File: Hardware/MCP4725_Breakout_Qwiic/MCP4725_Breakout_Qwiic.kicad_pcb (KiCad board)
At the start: 2 copper layers, 15.6 x 15.6 mm, 37 parts, among them J1 Conn_01x02, J2 I2C, U2 MCP4725

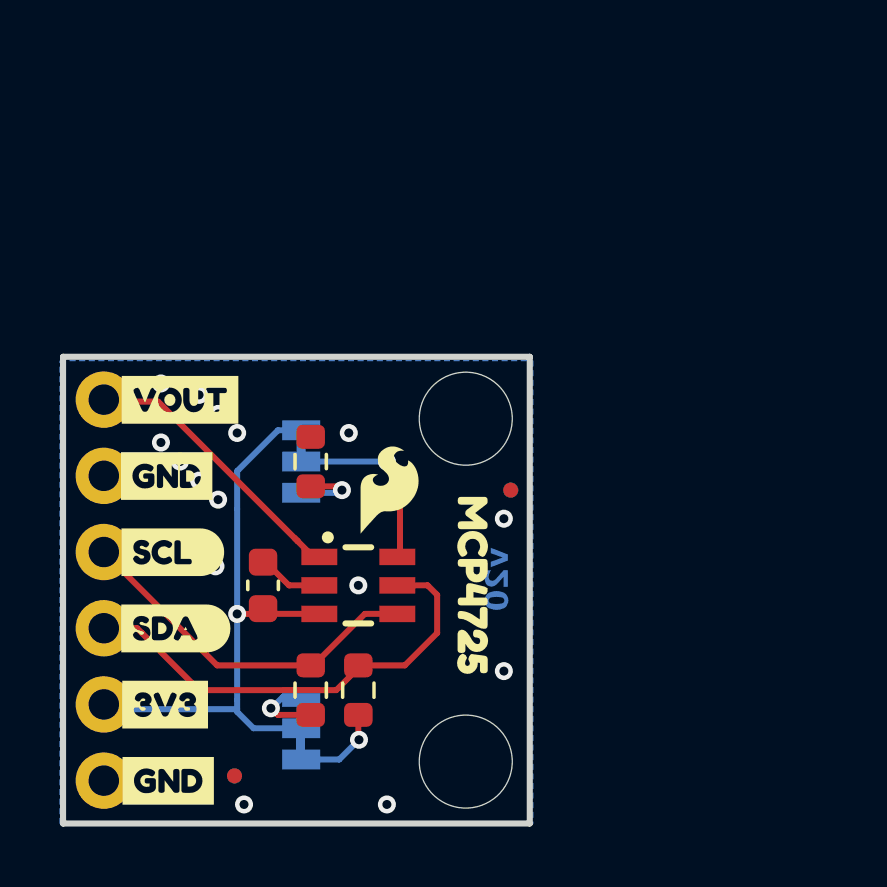
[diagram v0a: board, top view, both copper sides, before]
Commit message: Routes Qwiic Board, adds
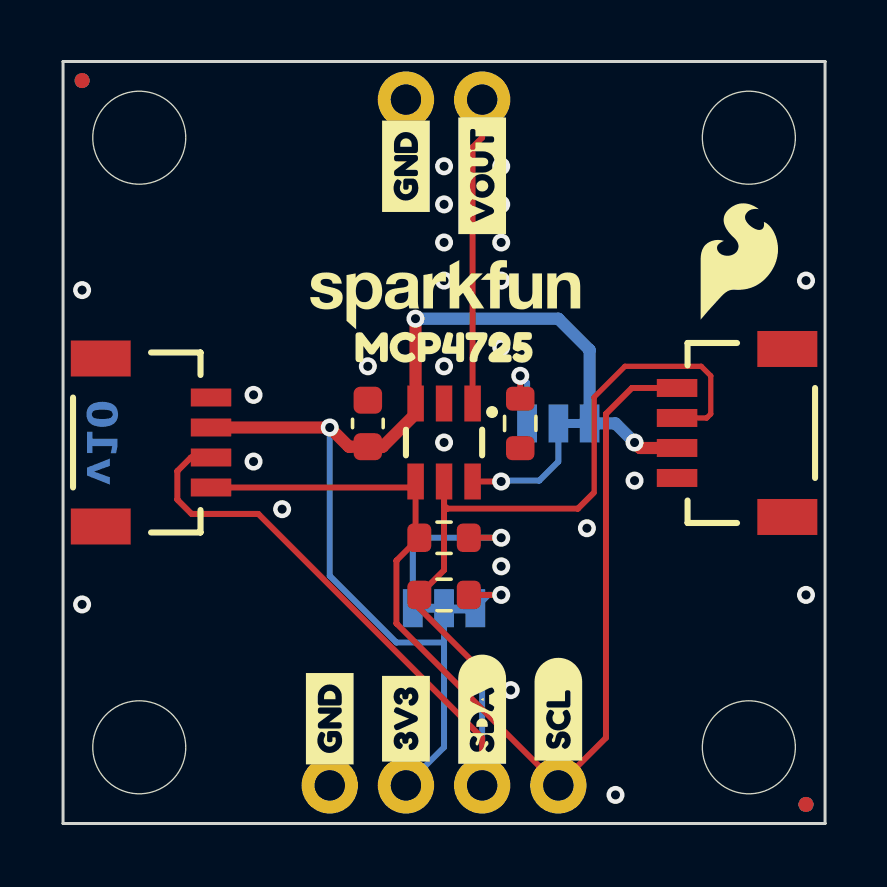
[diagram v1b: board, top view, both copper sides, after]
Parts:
- removed the G*** at (151.9, 101.3)
- removed the G*** at (154.8, 101.5)
- removed kibuzzard-69B46E88: G***, kibuzzard-69B46E88
- added G***: Flame, SparkFun-Aesthetic:SparkFun_Flame_4mm, F.Cu at (163.5, 93.7)
- added G***: LOGO, SparkFun-Aesthetic:SparkFun_Logo_NoFlame_9mm, F.Cu at (153.7, 94.6)
- added J3: Qwiic_RA, SparkFun-Connector:JST_1x04_P1.0mm_Horizontal_SMD, F.Cu at (161.4, 99.4)
- added J4: Qwiic_RA, SparkFun-Connector:JST_1x04_P1.0mm_Horizontal_SMD, F.Cu at (145.9, 99.7)
- added ST3: Standoff, SparkFun-Hardware:Standoff, F.Cu at (163.8, 89.5)
- added ST4: Standoff, SparkFun-Hardware:Standoff, F.Cu at (163.8, 109.9)
- added kibuzzard-69B9961C: G***, kibuzzard-69B9961C, B.Cu at (150.4, 105.3)
- moved FID1 19.8 mm to (141.6, 87.6), turned to -90 degrees
- moved FID2 19.8 mm to (141.6, 87.6), turned to 90 degrees
- moved FID3 19.1 mm to (165.7, 111.8), turned to 90 degrees
- moved FID4 19.1 mm to (165.7, 111.8), turned to -90 degrees
- moved J1 16.1 mm to (154.9, 88.3), turned to 180 degrees
- moved ST1 14.4 mm to (143.5, 89.5)
- moved kibuzzard-69B46E2A 13.9 mm to (157.5, 108.6), turned to 90 degrees
- moved kibuzzard-69B46EEC 13.9 mm to (157.5, 108.6), turned to -90 degrees
- moved kibuzzard-69B46D94 13.0 mm to (152.4, 90.5), turned to 90 degrees
- moved kibuzzard-69B46D94 13.0 mm to (152.4, 90.5), turned to -90 degrees
- moved kibuzzard-69B46D81 12.5 mm to (154.9, 90.8), turned to 90 degrees
- moved kibuzzard-69B46D81 12.5 mm to (154.9, 90.8), turned to -90 degrees
- moved kibuzzard-69B9770D 11.7 mm to (160.7, 99.1)
- moved ST2 10.9 mm to (143.5, 109.9)
- moved kibuzzard-69B46E2F 10.6 mm to (154.9, 108.6), turned to 90 degrees
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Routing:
- net SDA: track 15.4 -> 44.8 mm, vias 0 -> 1
- net SCL: track 12.1 -> 35.4 mm
- net 3.3V: track 20.7 -> 38.8 mm, vias 1 -> 3
- net Net-(JP1-A): track 2.76 -> 6.14 mm
- net GND: track 2.20 -> 0.00 mm, vias 15 -> 24
- net ADDR: track 6.18 -> 4.41 mm
- net Net-(JP1-C): track 2.95 -> 2.13 mm
- net VOUT: track 9.61 -> 10.3 mm
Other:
- board size 15.6 x 15.6 mm -> 25.4 x 25.4 mm
- board text added: "v10"
- board text removed: "v20"

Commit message: Adds measures, adds silk
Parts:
- removed kibuzzard-69B9961C: G***, kibuzzard-69B9961C
- added G***: LOGO, SparkFun-Aesthetic:SparkFun_Logo_10mm, B.Cu at (154.0, 95.6)
- added kibuzzard-69B9AECC: G***, kibuzzard-69B9AECC, B.Cu at (153.5, 103.4)
- moved kibuzzard-69B976CB 3.37 mm to (157.5, 100.8)
- moved kibuzzard-69B46E1A 3.17 mm to (153.7, 97.2)
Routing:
- net GND: vias 24 -> 26

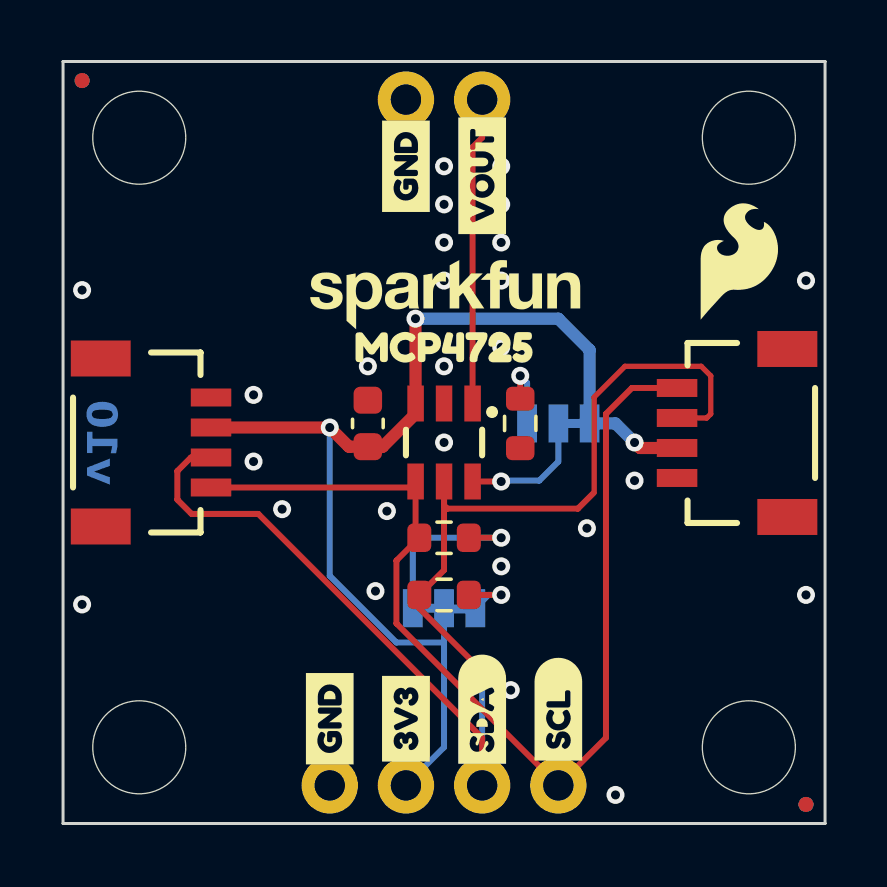
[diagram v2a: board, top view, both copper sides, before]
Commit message: Fixes DAC symbol, aligns Qwiic connector, removes extra pour
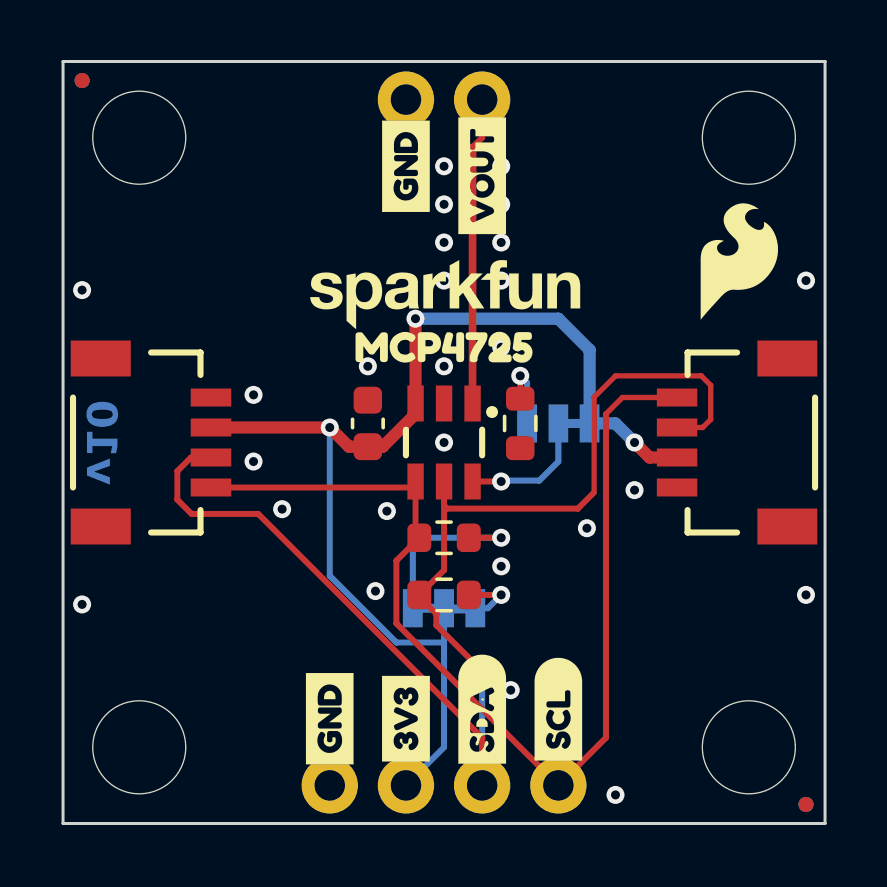
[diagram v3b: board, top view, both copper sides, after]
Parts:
- moved J3 0.32 mm to (161.4, 99.7)

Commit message: Fixes swapped pins on SCL/SDA
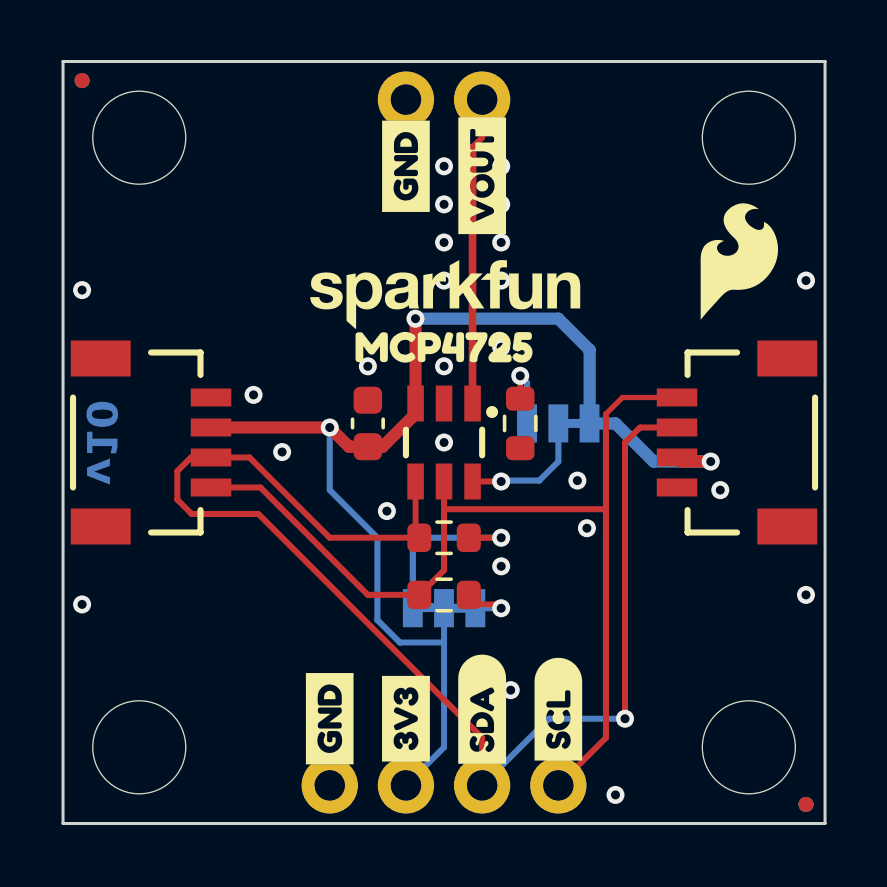
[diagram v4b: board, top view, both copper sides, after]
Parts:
- moved R4 1.91 mm to (153.7, 102.9)
- moved R5 1.91 mm to (153.7, 104.8)
- turned JP1 to 180 degrees
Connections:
- U2 pad 4: SCL -> SDA
- U2 pad 5: SDA -> SCL
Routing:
- net Net-(JP1-C): track 2.13 -> 6.14 mm
- net Net-(JP1-A): track 6.14 -> 2.13 mm
- net 3.3V: track 38.9 -> 41.2 mm
- net SCL: track 35.3 -> 33.6 mm
- net GND: vias 26 -> 25

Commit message: Adds new gitignore
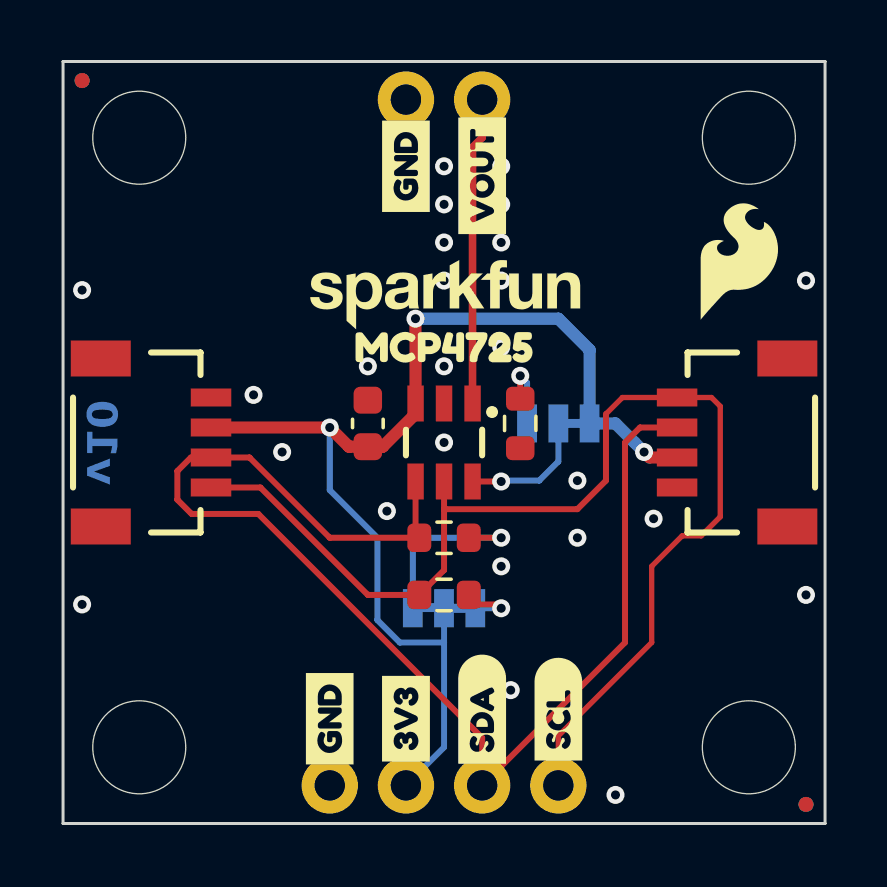
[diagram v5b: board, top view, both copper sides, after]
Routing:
- net SCL: track 33.6 -> 40.0 mm
- net 3.3V: track 41.2 -> 38.8 mm
- net SDA: track 44.1 -> 42.6 mm, vias 1 -> 0
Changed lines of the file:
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@@
 	)
 	(via
-		(at 162.8775 101.2825)
+		(at 160.655 102.235)
 		(size 0.6)
 		(drill 0.3)
@@
 	)
 	(via
-		(at 158.4325 102.5525)
+		(at 158.115 102.87)
 		(size 0.6)
 		(drill 0.3)
@@
 	)
 	(segment
-		(start 161.5725 100.33)
-		(end 161.4375 100.195)
-		(width 0.4064)
-		(layer "F.Cu")
-		(net 2)
-	)
-	(segment
 		(start 152.72 98.74)
 		(end 152.72 98.3949)
@@
 	)
 	(segment
+		(start 161.4375 100.195)
+		(end 160.52 100.195)
+		(width 0.4064)
+		(layer "F.Cu")
+		(net 2)
+	)
+	(segment
 		(start 151.13 99.835)
 		(end 150.5 99.835)
@@
 	)
 	(segment
-		(start 162.56 100.33)
-		(end 161.5725 100.33)
-		(width 0.4064)
-		(layer "F.Cu")
-		(net 2)
-	)
-	(segment
 		(start 151.13 99.835)
 		(end 151.625 99.835)
@@
 	)
 	(via
-		(at 162.56 100.33)
+		(at 160.3375 100.0125)
 		(size 0.6)
 		(drill 0.3)
@@
 	)
 	(segment
-		(start 160.02 99.695)
-		(end 160.655 100.33)
-		(width 0.4064)
-		(layer "B.Cu")
-		(net 2)
-	)
-	(segment
 		(start 159.385 99.06)
 		(end 160.02 99.695)
@@
 	)
 	(segment
-		(start 160.655 100.33)
-		(end 162.56 100.33)
-		(width 0.4064)
-		(layer "B.Cu")
-		(net 2)
-	)
-	(segment
 		(start 151.4475 105.6125)
 		(end 151.4475 102.87)
@@
 	)
 	(segment
+		(start 160.02 99.695)
+		(end 160.52 100.195)
+		(width 0.4064)
+		(layer "B.Cu")
+		(net 2)
+	)
+	(segment
 		(start 157.48 95.5675)
 		(end 158.5214 96.6089)
@@
 	)
 	(segment
+		(start 159.0675 100.965)
+		(end 159.0675 98.7425)
+		(width 0.2)
+		(layer "F.Cu")
+		(net 3)
+	)
+	(segment
 		(start 159.615 98.195)
 		(end 159.0675 98.7425)
@@
 	)
 	(segment
-		(start 159.0675 101.9175)
-		(end 159.0675 98.7425)
+		(start 162.8775 102.1715)
+		(end 162.2425 102.8065)
+		(width 0.1778)
+		(layer "F.Cu")
+		(net 3)
+	)
+	(segment
+		(start 161.4375 98.195)
+		(end 162.584 98.195)
+		(width 0.1778)
+		(layer "F.Cu")
+		(net 3)
+	)
+	(segment
+		(start 158.115 101.9175)
+		(end 159.0675 100.965)
 		(width 0.2)
 		(layer "F.Cu")
@@
 	)
 	(segment
-		(start 159.0675 109.5375)
-		(end 159.0675 101.9175)
-		(width 0.2)
+		(start 162.8775 98.4885)
+		(end 162.8775 102.1715)
+		(width 0.1778)
 		(layer "F.Cu")
 		(net 3)
@@
 	)
 	(segment
+		(start 153.67 101.9175)
+		(end 158.115 101.9175)
+		(width 0.2)
+		(layer "F.Cu")
+		(net 3)
+	)
+	(segment
+		(start 161.6075 102.8065)
+		(end 160.5915 103.8225)
+		(width 0.1778)
+		(layer "F.Cu")
+		(net 3)
+	)
+	(segment
+		(start 157.48 109.474)
+		(end 157.48 111.125)
+		(width 0.1778)
+		(layer "F.Cu")
+		(net 3)
+	)
+	(segment
+		(start 160.5915 106.3625)
+		(end 157.48 109.474)
+		(width 0.1778)
+		(layer "F.Cu")
+		(net 3)
+	)
+	(segment
 		(start 147.55 101.195)
 		(end 145.9025 101.195)
@@
 	)
 	(segment
-		(start 153.67 101.9175)
-		(end 159.0675 101.9175)
-		(width 0.2)
-		(layer "F.Cu")
-		(net 3)
-	)
-	(segment
-		(start 157.48 111.125)
-		(end 159.0675 109.5375)
-		(width 0.2)
+		(start 162.2425 102.8065)
+		(end 161.6075 102.8065)
+		(width 0.1778)
+		(layer "F.Cu")
+		(net 3)
+	)
+	(segment
+		(start 162.584 98.195)
+		(end 162.8775 98.4885)
+		(width 0.1778)
 		(layer "F.Cu")
 		(net 3)
@@
 	)
 	(segment
-		(start 159.7025 108.9025)
+		(start 160.5915 103.8225)
+		(end 160.5915 106.3625)
+		(width 0.1778)
+		(layer "F.Cu")
+		(net 3)
+	)
+	(segment
+		(start 159.7025 106.3625)
 		(end 159.7025 99.695)
 		(width 0.2)
@@
 	)
 	(segment
+		(start 154.94 111.125)
+		(end 159.7025 106.3625)
+		(width 0.2)
+		(layer "F.Cu")
+		(net 4)
+	)
+	(segment
 		(start 160.2025 99.195)
 		(end 159.7025 99.695)
@@
 		(width 0.2)
 		(layer "F.Cu")
-		(net 4)
-	)
-	(via
-		(at 159.7025 108.9025)
-		(size 0.6)
-		(drill 0.3)
-		(layers "F.Cu" "B.Cu")
-		(net 4)
-	)
-	(segment
-		(start 157.48 108.9025)
-		(end 159.7025 108.9025)
-		(width 0.2)
-		(layer "B.Cu")
-		(net 4)
-	)
-	(segment
-		(start 154.94 111.125)
-		(end 157.1625 108.9025)
-		(width 0.2)
-		(layer "B.Cu")
-		(net 4)
-	)
-	(segment
-		(start 157.1625 108.9025)
-		(end 157.48 108.9025)
-		(width 0.2)
-		(layer "B.Cu")
 		(net 4)
 	)
@@
 		(start 154.94 89.5325)
 		(end 154.62 89.8525)
-		(width 0.2)
+		(width 0.254)
 		(layer "F.Cu")
 		(net 8)
@@
 		(start 154.94 88.265)
 		(end 154.94 89.5325)
-		(width 0.2)
+		(width 0.254)
 		(layer "F.Cu")
 		(net 8)

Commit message: Adds Qwiic Logo, power LED, adds "DAC" to product silk
* Fixes the address jumper
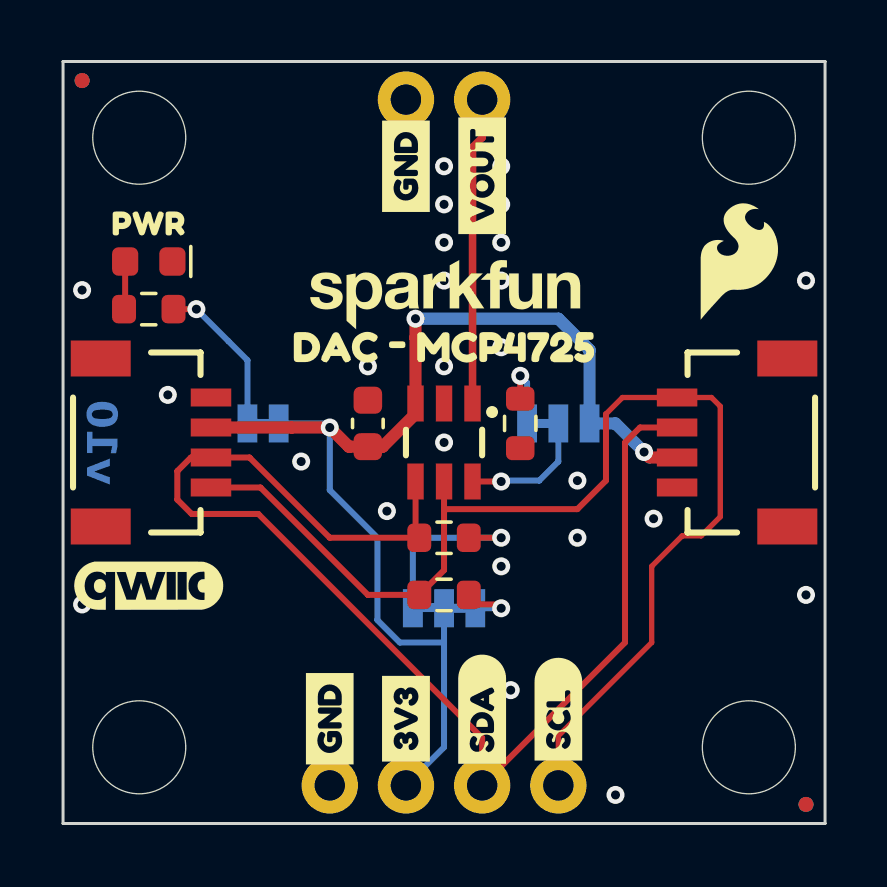
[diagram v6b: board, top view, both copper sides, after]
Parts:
- removed the G*** at (154.0, 95.6)
- removed kibuzzard-69B46E1A (x2): G***, kibuzzard-69B46E1A
- removed kibuzzard-69B976CB: G***, kibuzzard-69B976CB
- removed kibuzzard-69B9AECC: G***, kibuzzard-69B9AECC
- added D1: Red, SparkFun-LED:LED_0603_1608Metric_Red, F.Cu at (143.8, 93.7)
- added G***: LOGO, SparkFun-Aesthetic:qwiic_5mm, F.Cu at (143.8, 104.5)
- added G***: Flame, SparkFun-Aesthetic:SparkFun_Flame_4mm, B.Cu at (149.5, 91.4)
- added G***: LOGO, SparkFun-Aesthetic:SparkFun_Logo_NoFlame_9mm, B.Cu at (153.7, 94.0)
- added JP3: LED, SparkFun-Jumper:Jumper_2_NC_Trace, B.Cu at (147.6, 99.1)
- added R2: 4.7k, SparkFun-Resistor:R_0603_1608Metric, F.Cu at (143.8, 95.2)
- added kibuzzard-69BC0473: G***, kibuzzard-69BC0473, F.Cu at (153.7, 96.5)
- added kibuzzard-69BC04C8: G***, kibuzzard-69BC04C8, F.Cu at (143.8, 92.4)
- added kibuzzard-69BC0544: G***, kibuzzard-69BC0544, B.Cu at (153.5, 95.8)
- added kibuzzard-69BC0559: G***, kibuzzard-69BC0559, B.Cu at (157.5, 100.7)
- added kibuzzard-69BC0561: G***, kibuzzard-69BC0561, B.Cu at (147.6, 100.7)
- added kibuzzard-69BC0567: G***, kibuzzard-69BC0567, B.Cu at (153.7, 103.6)
- turned JP2 to 0 degrees
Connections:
- JP2 pad 1: 3.3V -> Net-(JP2-A)
- JP2 pad 3: Net-(JP2-C) -> 3.3V
- R1 pad 2: Net-(JP2-C) -> Net-(JP2-A)
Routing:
- net Net-(JP3-A): track 0.00 -> 5.28 mm, vias 0 -> 1
- net Net-(JP2-C): track 2.44 -> 0.00 mm, vias 1 -> 0
- net Net-(JP2-A): track 0.00 -> 2.44 mm, vias 0 -> 1
- net 3.3V: track 38.8 -> 40.6 mm
- net Net-(D1-A): track 0.00 -> 1.60 mm
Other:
- board text added: "Finish: HASL Lead-Free"
- board text added: "Layers: 2"
- board text added: "Material: TG135"
- board text added: "Ordering Notes"
- board text added: "Outer Copper Weight: 1oz"
- board text added: "Silkscreen Color: White"
- board text added: "Solder Mask: Red"
- board text added: "Thickness: 1.6mm"
